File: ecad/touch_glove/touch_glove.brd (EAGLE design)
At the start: 78.3 x 40.6 mm, 177 parts, among them Q1 MCH3474 4A/30V, Q2 MCH3474 4A/30V, Q3 MCH3474 4A/30V, Q4 MCH3474 4A/30V, Q5 MCH3474 4A/30V, Q6 MCH3474 4A/30V, SW1 4A/28V

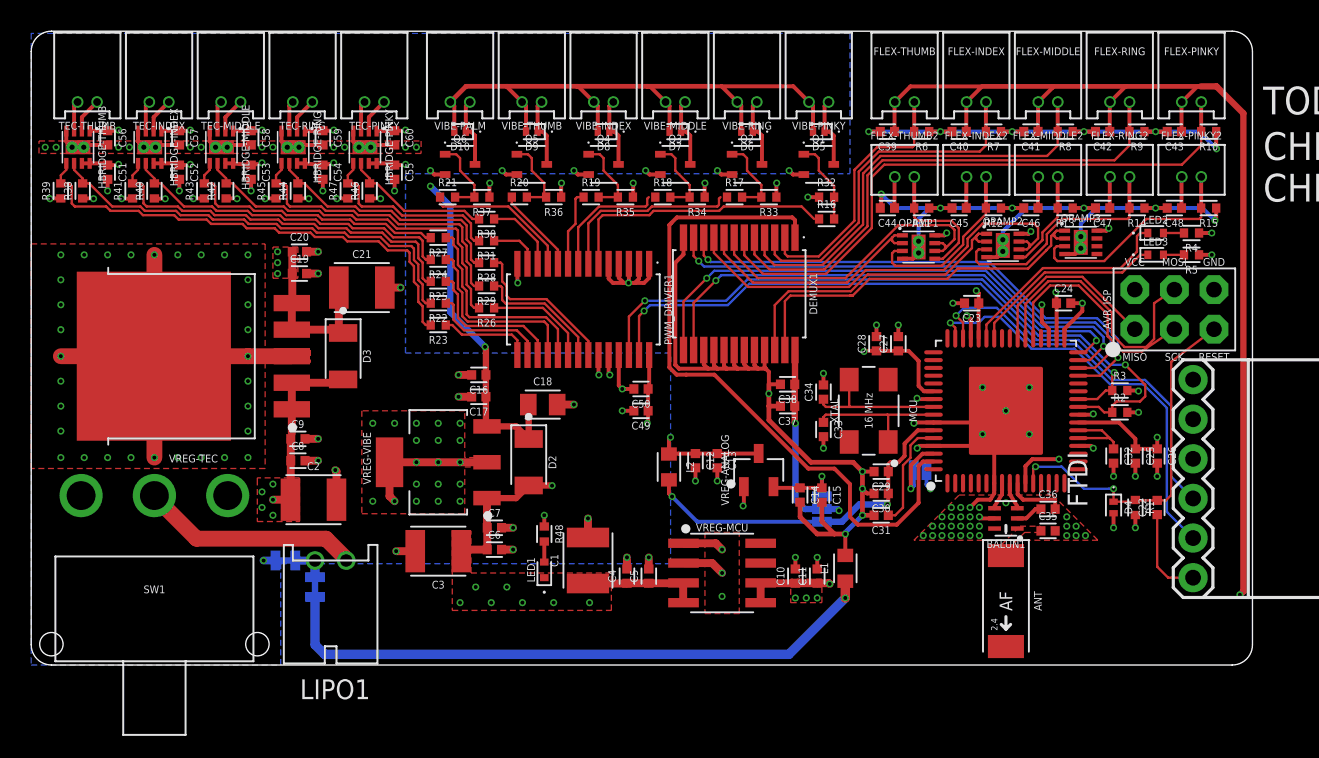
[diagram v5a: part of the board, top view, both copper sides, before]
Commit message: Update all components to new libraries.
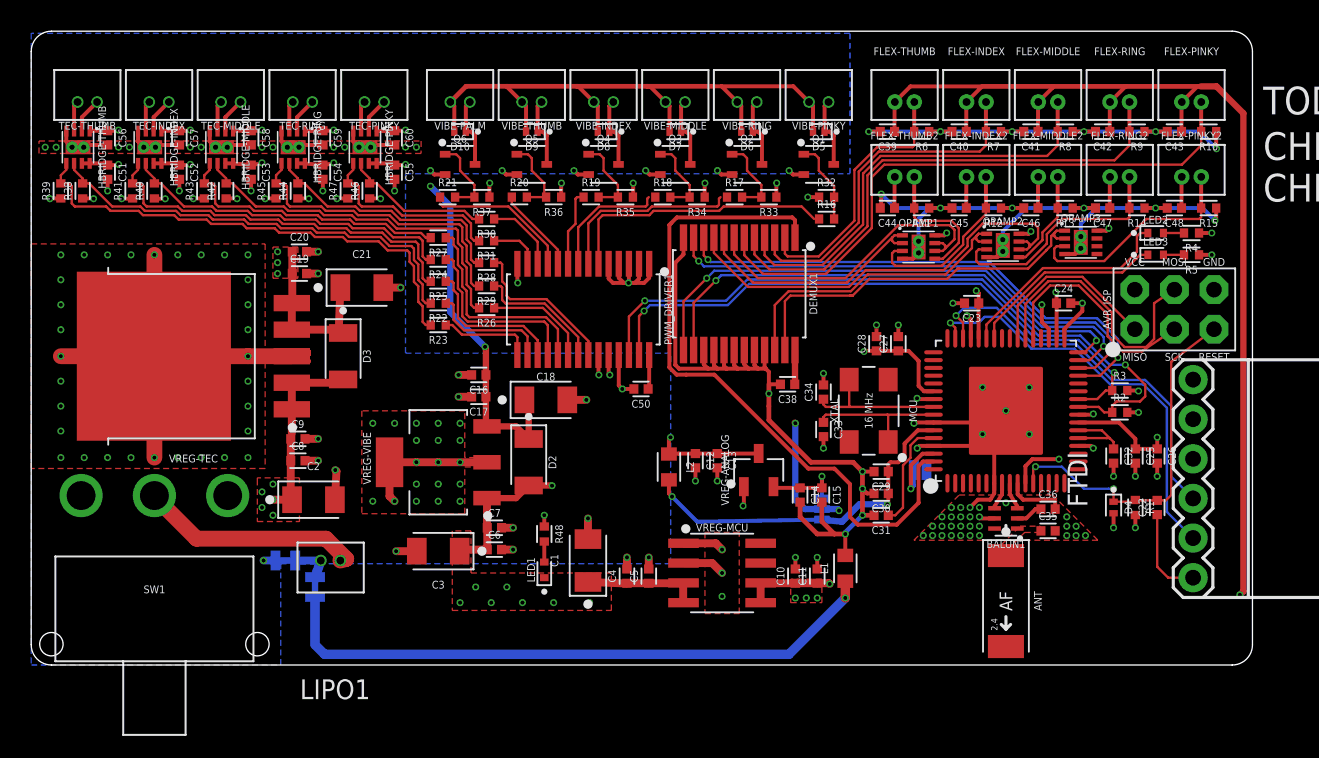
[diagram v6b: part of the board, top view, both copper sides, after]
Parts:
- removed C37, C49: 10uF/6.3V, PiB_capacitors:CAPC1005X55_SMD-0402
- ANT: device PiB_radio_frequency:ANTC6522X100 -> _radio_frequency:ANTC6522X100
- AVR_ISP: device PiB_connectors:HDRV6W64P254_2X3_762X483X838B_AVR-ISP -> _connectors:HDRV6W64P254_2X3_762X483X838B_AVR-ISP
- BALUN1: device PiB_radio_frequency:RESCAXE65P200X125X95-6 -> _radio_frequency:RESCAXE65P200X125X95-6
- BR_ANALOG, BR_NOISE: value 2PT_GND_TIE -> NET_BRIDGE; device PiB_power_symbols:2PT_GND_TIE -> _power_symbols:NET_BRIDGE
- C1, C2, C21, C3: device PiB_capacitors:CAPC3225X270_SMD-1210 -> _capacitors:CAPCP3216X160
- C10, C11, C12, C13, C14, C15, C16, C17, C19, C20, C22, C23, C24, C25, C26, C27, C28, C29, C30, C31, C32, C33, C34, C35, C36, C38, C39, C4, C40, C41, C42, C43, C44, C45, C46, C47, C48, C5, C50, C51, C52, C53, C54, C55, C56, C57, C58, C59, C6, C60, C7, C8, C9: device PiB_capacitors:CAPC1005X55_SMD-0402 -> _capacitors:CAPC1005X55_SMD-0402
- C18: value 47uF/6.3V -> 100uF/10V; device PiB_capacitors:CAPC2012X95_SMD-0805 -> _capacitors:CAPCP3216X160
- D10, D4, D5, D6, D7, D8, D9: device PiB_discrete_semiconductors:DFN100X60X55-2 -> _discrete_semiconductors:DFN100X60X55-2
- D2, D3: device PiB_discrete_semiconductors:SODFL3516X170 -> _discrete_semiconductors:SODFL3516X170
- DEMUX1: device PiB:SOP65P780X200-24 -> _special:SOP65P780X200-24
- FLEX-INDEX, FLEX-MIDDLE, FLEX-PINKY, FLEX-RING, FLEX-THUMB: device PiB_sensors:_MOLEX-0530480210_RA_PITCH-1.25MM -> _sensors:_MOLEX-0530470210_VERT_PITCH-1.25MM
- FLEX-INDEX2, FLEX-MIDDLE2, FLEX-PINKY2, FLEX-RING2, FLEX-THUMB2: device PiB_sensors:_MOLEX-0530470210_VERT_PITCH-1.25MM -> _sensors:_MOLEX-0530470210_VERT_PITCH-1.25MM
- FTDI: device PiB_connectors:FTDI_BASIC-6PIN-MALE-RA -> _connectors:FTDI_BASIC-6PIN-MALE-RA
- HBRIDGE-INDEX, HBRIDGE-MIDDLE, HBRIDGE-PINKY, HBRIDGE-RING, HBRIDGE-THUMB: device PiB:WSON-8-PPAD -> _special:WSON-8-PPAD
- JP1: value JUMPER_SMD_3-PAD_NO_NO-SILK -> JUMPER_SMD_3-PAD_NO_SILK; device PiB_connectors:SMT-JUMPER_3_NO_NO-SILK -> _connectors:SMT-JUMPER_3_NO_SILK
- JP2: device PiB_connectors:SMT-JUMPER_2_NO_SILK -> _connectors:SMT-JUMPER_2_NO_SILK
- L1, L2: device PiB_inductors:INDC1608X60-0603 -> _inductors:INDC1608X60-0603
- LED1, LED2, LED3: device PiB_leds:LEDC1005X40_LED-0402 -> _leds:LEDC1005X40_LED-0402
- LIPO1: device PiB_batteries:BATTERY_MOLEX-89401_RA_PITCH-2MM -> _batteries:BATTERY_MOLEX-0530470210_VERT_PITCH-1.25MM
- MCU: device PiB_ic_microcontrollers:QFN50P900X900X90-64 -> _ic_microcontrollers:QFN50P900X900X90-64
- OPAMP1, OPAMP2, OPAMP3: device PiB_op_amps:WSON-8-PPAD -> _op_amps:WSON-8-PPAD
- PWM_DRIVER1: device PiB:SOP65P650X110-28 -> _special:SOP65P650X110-28
- Q1, Q2, Q3, Q4, Q5, Q6: device PiB_discrete_semiconductors:SOTFL65P209X90-3 -> _transistors:SOTFL65P209X90-3
- R1, R10, R11, R12, R13, R14, R15, R16, R17, R18, R19, R2, R20, R21, R22, R23, R24, R25, R26, R27, R28, R29, R3, R30, R31, R32, R33, R34, R35, R36, R37, R38, R39, R4, R40, R41, R42, R43, R44, R45, R46, R47, R48, R5, R6, R7, R8, R9: device PiB_resistors:RESC1005X35_SMD-0402 -> _resistors:RESC1005X35_SMD-0402
- SW1: device PiB_switches:SW_SLIDE_SPDT_RA_PTH_12.7L-9.5W -> _switches:SW_SLIDE_SPDT_RA_PTH_12.7L-9.5W
- TEC-INDEX, TEC-MIDDLE, TEC-PINKY, TEC-RING, TEC-THUMB: value Molex RA 1.25mm pitch -> PELTIER; device PiB_actuators:_MOLEX-0530480210_RA_PITCH-1.25MM -> _actuators:_MOLEX-0530470210_VERT_PITCH-1.25MM
- VIBE-INDEX, VIBE-MIDDLE, VIBE-PALM, VIBE-PINKY, VIBE-RING, VIBE-THUMB: value Molex RA 1.25mm pitch -> Molex VERT 1.25mm pitch; device PiB_actuators:_MOLEX-0530480210_RA_PITCH-1.25MM -> _actuators:_MOLEX-0530470210_VERT_PITCH-1.25MM
- VREG-ANALOG: device PiB_ic_power:SOT95P237X112-3_SOT-23-3 -> _ic_power:SOT95P237X112-3_SOT-23-3
- VREG-MCU: value 1A/3.3V -> TPS76833QDR 1A/3.3V; device PiB_ic_power:SOIC127P600X265-8 -> _ic_power:SOIC127P600X265-8
- VREG-TEC: device PiB_ic_power:TO170P1363X457-6 -> _ic_power:TO170P1363X457-6
- VREG-VIBE: device PiB_ic_power:SOT229P700X180-4 -> _ic_power:SOT229P700X180-4
- XTAL: device PiB:OSCCC500X320X110 -> _crystals_oscillators_resonators:OSCCC500X320X110_CRYSTAL
- moved C18 0.36 mm to (33.0, 17.0)
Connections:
- net 1.8V: now also C21.A; no longer C21.1
- net 3.3V: now also C18.A; no longer C18.1
- net AGND: no longer C37.2
- net GND: no longer C49.2
- net NGND: now also C1.K, C18.K, C2.K, C21.K, C3.K; no longer C1.2, C18.2, C2.2, C21.2, C3.2
- net VBAT: now also C1.A, C2.A, C3.A; no longer C1.1, C2.1, C3.1
- net VCC: no longer C49.1
- net VSENSOR: no longer C37.1
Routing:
- net VSENSOR: track 178.9 -> 176.5 mm
- net VCC: track 51.7 -> 49.4 mm, vias 19 -> 18
- net AGND: track 227.7 -> 227.0 mm
- net 3.3V: track 70.0 -> 70.5 mm
- net GND: track 66.1 -> 65.8 mm, vias 52 -> 51

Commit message: Fix all errors on board.
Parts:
- moved AVR_ISP 0.10 mm to (70.8, 21.4)
- moved C17 0.10 mm to (28.7, 17.3)
- moved FLEX-INDEX 0.10 mm to (60.6, 36.2)
- moved FLEX-MIDDLE 0.10 mm to (65.2, 36.2)
- moved FLEX-PINKY 0.10 mm to (74.4, 36.2)
- moved FLEX-RING 0.10 mm to (69.8, 36.2)
- moved FLEX-THUMB 0.10 mm to (56.0, 36.2)
- moved TEC-INDEX 0.10 mm to (8.20, 36.2)
- moved TEC-MIDDLE 0.10 mm to (12.8, 36.2)
- moved TEC-PINKY 0.10 mm to (22.0, 36.2)
- moved TEC-RING 0.10 mm to (17.4, 36.2)
- moved TEC-THUMB 0.10 mm to (3.60, 36.2)
- moved VIBE-INDEX 0.10 mm to (36.7, 36.2)
- moved VIBE-MIDDLE 0.10 mm to (41.3, 36.2)
- moved VIBE-PALM 0.10 mm to (27.5, 36.2)
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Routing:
- net VSENSOR: track 176.5 -> 180.0 mm
- net VCC: track 49.4 -> 50.3 mm, vias 18 -> 19
- net 3.3V: track 70.5 -> 71.2 mm

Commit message: Completed most of the circuitry for the ET schematic.
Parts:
- added C37, C49, C63, C64, C66, C67, C68, C69, C70, C76, C78, C80: 0.1uF/50V, _capacitors:CAPC1005X55_SMD-0402
- added C61: 0.1uF/25V, _capacitors:CAPC1608X95
- added C62: 0.1uF/250V, _capacitors:CAPC2012X95_SMD-0805
- added C65: 100uF/10V, _capacitors:CAPCP3216X160
- added C71, C72, C73, C75, C77, C79: 10uF/6.3V, _capacitors:CAPC1005X55_SMD-0402
- added C74: 4.7uF/10V/0402, _capacitors:CAPC1005X55_SMD-0402
- added ET_INDEX_PIXEL1-1, ET_INDEX_PIXEL1-10, ET_INDEX_PIXEL1-11, ET_INDEX_PIXEL1-12, ET_INDEX_PIXEL1-13, ET_INDEX_PIXEL1-14, ET_INDEX_PIXEL1-15, ET_INDEX_PIXEL1-16, ET_INDEX_PIXEL1-17, ET_INDEX_PIXEL1-18, ET_INDEX_PIXEL1-19, ET_INDEX_PIXEL1-2, ET_INDEX_PIXEL1-20, ET_INDEX_PIXEL1-3, ET_INDEX_PIXEL1-4, ET_INDEX_PIXEL1-5, ET_INDEX_PIXEL1-6, ET_INDEX_PIXEL1-7, ET_INDEX_PIXEL1-8, ET_INDEX_PIXEL1-9, ET_INDEX_PIXEL2-1, ET_INDEX_PIXEL2-10, ET_INDEX_PIXEL2-11, ET_INDEX_PIXEL2-12, ET_INDEX_PIXEL2-13, ET_INDEX_PIXEL2-14, ET_INDEX_PIXEL2-15, ET_INDEX_PIXEL2-16, ET_INDEX_PIXEL2-17, ET_INDEX_PIXEL2-18, ET_INDEX_PIXEL2-19, ET_INDEX_PIXEL2-2, ET_INDEX_PIXEL2-20, ET_INDEX_PIXEL2-3, ET_INDEX_PIXEL2-4, ET_INDEX_PIXEL2-5, ET_INDEX_PIXEL2-6, ET_INDEX_PIXEL2-7, ET_INDEX_PIXEL2-8, ET_INDEX_PIXEL2-9, ET_INDEX_PIXEL3-1, ET_INDEX_PIXEL3-10, ET_INDEX_PIXEL3-11, ET_INDEX_PIXEL3-12, ET_INDEX_PIXEL3-13, ET_INDEX_PIXEL3-14, ET_INDEX_PIXEL3-15, ET_INDEX_PIXEL3-16, ET_INDEX_PIXEL3-17, ET_INDEX_PIXEL3-18, ET_INDEX_PIXEL3-19, ET_INDEX_PIXEL3-2, ET_INDEX_PIXEL3-20, ET_INDEX_PIXEL3-3, ET_INDEX_PIXEL3-4, ET_INDEX_PIXEL3-5, ET_INDEX_PIXEL3-6, ET_INDEX_PIXEL3-7, ET_INDEX_PIXEL3-8, ET_INDEX_PIXEL3-9, ET_INDEX_PIXEL4-1, ET_INDEX_PIXEL4-10, ET_INDEX_PIXEL4-11, ET_INDEX_PIXEL4-12, ET_INDEX_PIXEL4-13, ET_INDEX_PIXEL4-14, ET_INDEX_PIXEL4-15, ET_INDEX_PIXEL4-16, ET_INDEX_PIXEL4-17, ET_INDEX_PIXEL4-18, ET_INDEX_PIXEL4-19, ET_INDEX_PIXEL4-2, ET_INDEX_PIXEL4-20, ET_INDEX_PIXEL4-3, ET_INDEX_PIXEL4-4, ET_INDEX_PIXEL4-5, ET_INDEX_PIXEL4-6, ET_INDEX_PIXEL4-7, ET_INDEX_PIXEL4-8, ET_INDEX_PIXEL4-9: SPST-NO 170mA 250V, _relay:SOP254P609X203-4
- added IC1: DRV8662, _special:QFN50P400X400X100-21T270
- added J1, J2, J3, J4, J5: VERT MALE 2.54MM, _connectors:HDRV16W64P254_1X16_4064X254X838B
- added J6, J7, J8, J9: PTH VERT MALE, _connectors:HDRV2W64P254_1X2_508X254X838B
- added L3: 4.7uH/1.4A, _inductors:INDC2520X100
- added L4: 10uH/380mA, _inductors:INDC1608X60-0603
- added NFET1: 2N7002DW, _transistors:SOT65P230X110-6
- added OPAMP4: TLV2361_GP_20MA_7MHZ, _op_amps:SOT95P280X145-5
- added POT1: 100K, _resistors:POTENTIOMETER_SQ-L5-W4.5-H2.3
- added PWM_DRIVER2, PWM_DRIVER3, PWM_DRIVER4, PWM_DRIVER5, PWM_DRIVER6: PCA9685, _special:SOP65P650X110-28
- added R100, R101, R102, R103, R104, R105, R106, R107, R108, R109, R110, R111, R112, R113, R114, R115, R116, R117, R118, R119, R120, R121, R122, R123, R124, R125, R126, R127, R128, R129, R130, R131, R132, R133, R134, R135, R49, R57, R58, R59, R60, R61, R62, R63, R64, R65, R66, R67, R68, R69, R70, R71, R72, R73, R74, R75, R76, R77, R78, R79, R80, R81, R82, R83, R84, R85, R86, R87, R88, R89, R90, R91, R92, R93, R94, R95, R96, R97, R98, R99: 1K, _resistors:RESC1005X35_SMD-0402
- added R136, R137, R54, R55, R56: 10K, _resistors:RESC1005X35_SMD-0402
- added R50: 768K, _resistors:RESC1005X35_SMD-0402
- added R51: 35.7K, _resistors:RESC1005X35_SMD-0402
- added R52: 20K, _resistors:RESC1005X35_SMD-0402
- added R53: 41.2K, _resistors:RESC1005X35_SMD-0402
- added REXT: 7.5K, _resistors:RESC1005X35_SMD-0402
- added SW2: 25mA/24V, _switches:SW_SLIDE_ARRAY-3_L9.6-W7.5-H4.5
- added VREG-MCU1: TPS76833QDR 1A/3.3V, _ic_power:SOIC127P600X265-8
- added VREG2: NCP1729 50mA, _ic_power:SOT95P275X100-6
- added VREG3: TPS62202 300mA 1.8V, _ic_power:SOT95P280X145-5
- moved C21 0.57 mm to (20.8, 23.8)
- moved D3 0.40 mm to (19.6, 19.8)
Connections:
- new net -1.8V: C72.1, OPAMP4.2, VREG2.1
- new net C+: C71.1, VREG2.6
- new net C-: C71.2, VREG2.3
- new net EN: IC1.20, R54.2, SW2.S3
- new net FB: IC1.3, R50.1, R51.2, R52.2, R53.2
- new net GAIN0: IC1.18, NFET1.5, R55.2, SW2.S2
- new net GAIN1: IC1.19, NFET1.2, R56.2, SW2.S1
- new net IN+: C64.1, OPAMP4.4, POT1.1, POT1.2, R136.2
- new net INDEX_IN1-1: ET_INDEX_PIXEL1-1.1, ET_INDEX_PIXEL1-13.1, ET_INDEX_PIXEL1-17.1, ET_INDEX_PIXEL1-5.1, ET_INDEX_PIXEL1-9.1, PWM_DRIVER2.6, PWM_DRIVER3.6, PWM_DRIVER4.6, PWM_DRIVER5.6, PWM_DRIVER6.6
- new net INDEX_IN1-2: ET_INDEX_PIXEL1-10.1, ET_INDEX_PIXEL1-14.1, ET_INDEX_PIXEL1-18.1, ET_INDEX_PIXEL1-2.1, ET_INDEX_PIXEL1-6.1, PWM_DRIVER2.7, PWM_DRIVER3.7, PWM_DRIVER4.7, PWM_DRIVER5.7, PWM_DRIVER6.7
- new net INDEX_IN1-3: ET_INDEX_PIXEL1-11.1, ET_INDEX_PIXEL1-15.1, ET_INDEX_PIXEL1-19.1, ET_INDEX_PIXEL1-3.1, ET_INDEX_PIXEL1-7.1, PWM_DRIVER2.8, PWM_DRIVER3.8, PWM_DRIVER4.8, PWM_DRIVER5.8, PWM_DRIVER6.8
- new net INDEX_IN1-4: ET_INDEX_PIXEL1-12.1, ET_INDEX_PIXEL1-16.1, ET_INDEX_PIXEL1-20.1, ET_INDEX_PIXEL1-4.1, ET_INDEX_PIXEL1-8.1, PWM_DRIVER2.9, PWM_DRIVER3.9, PWM_DRIVER4.9, PWM_DRIVER5.9, PWM_DRIVER6.9
- new net INDEX_IN2-1: ET_INDEX_PIXEL2-1.1, ET_INDEX_PIXEL2-11.1, ET_INDEX_PIXEL2-15.1, ET_INDEX_PIXEL2-19.1, ET_INDEX_PIXEL2-7.1, PWM_DRIVER2.10, PWM_DRIVER3.10, PWM_DRIVER4.10, PWM_DRIVER5.10, PWM_DRIVER6.10
- new net INDEX_IN2-2: ET_INDEX_PIXEL2-10.1, ET_INDEX_PIXEL2-14.1, ET_INDEX_PIXEL2-18.1, ET_INDEX_PIXEL2-2.1, ET_INDEX_PIXEL2-6.1, PWM_DRIVER2.11, PWM_DRIVER3.11, PWM_DRIVER4.11, PWM_DRIVER5.11, PWM_DRIVER6.11
- new net INDEX_IN2-3: ET_INDEX_PIXEL2-13.1, ET_INDEX_PIXEL2-17.1, ET_INDEX_PIXEL2-3.1, ET_INDEX_PIXEL2-5.1, ET_INDEX_PIXEL2-9.1, PWM_DRIVER2.12, PWM_DRIVER3.12, PWM_DRIVER4.12, PWM_DRIVER5.12, PWM_DRIVER6.12
- new net INDEX_IN2-4: ET_INDEX_PIXEL2-12.1, ET_INDEX_PIXEL2-16.1, ET_INDEX_PIXEL2-20.1, ET_INDEX_PIXEL2-4.1, ET_INDEX_PIXEL2-8.1, PWM_DRIVER2.13, PWM_DRIVER3.13, PWM_DRIVER4.13, PWM_DRIVER5.13, PWM_DRIVER6.13
- new net INDEX_IN3-1: ET_INDEX_PIXEL3-1.1, ET_INDEX_PIXEL3-13.1, ET_INDEX_PIXEL3-17.1, ET_INDEX_PIXEL3-5.1, ET_INDEX_PIXEL3-9.1, PWM_DRIVER2.15, PWM_DRIVER3.15, PWM_DRIVER4.15, PWM_DRIVER5.15, PWM_DRIVER6.15
- new net INDEX_IN3-2: ET_INDEX_PIXEL3-10.1, ET_INDEX_PIXEL3-14.1, ET_INDEX_PIXEL3-18.1, ET_INDEX_PIXEL3-2.1, ET_INDEX_PIXEL3-6.1, PWM_DRIVER2.16, PWM_DRIVER3.16, PWM_DRIVER4.16, PWM_DRIVER5.16, PWM_DRIVER6.16
- new net INDEX_IN3-3: ET_INDEX_PIXEL3-11.1, ET_INDEX_PIXEL3-15.1, ET_INDEX_PIXEL3-19.1, ET_INDEX_PIXEL3-3.1, ET_INDEX_PIXEL3-7.1, PWM_DRIVER2.17, PWM_DRIVER3.17, PWM_DRIVER4.17, PWM_DRIVER5.17, PWM_DRIVER6.17
- new net INDEX_IN3-4: ET_INDEX_PIXEL3-12.1, ET_INDEX_PIXEL3-16.1, ET_INDEX_PIXEL3-20.1, ET_INDEX_PIXEL3-4.1, ET_INDEX_PIXEL3-8.1, PWM_DRIVER2.18, PWM_DRIVER3.18, PWM_DRIVER4.18, PWM_DRIVER5.18, PWM_DRIVER6.18
- new net INDEX_IN4-1: ET_INDEX_PIXEL4-1.1, ET_INDEX_PIXEL4-13.1, ET_INDEX_PIXEL4-17.1, ET_INDEX_PIXEL4-5.1, ET_INDEX_PIXEL4-9.1, PWM_DRIVER2.19, PWM_DRIVER3.19, PWM_DRIVER4.19, PWM_DRIVER5.19, PWM_DRIVER6.19
- new net INDEX_IN4-2: ET_INDEX_PIXEL4-10.1, ET_INDEX_PIXEL4-14.1, ET_INDEX_PIXEL4-18.1, ET_INDEX_PIXEL4-2.1, ET_INDEX_PIXEL4-6.1, PWM_DRIVER2.20, PWM_DRIVER3.20, PWM_DRIVER4.20, PWM_DRIVER5.20, PWM_DRIVER6.20
- new net INDEX_IN4-3: ET_INDEX_PIXEL4-11.1, ET_INDEX_PIXEL4-15.1, ET_INDEX_PIXEL4-19.1, ET_INDEX_PIXEL4-3.1, ET_INDEX_PIXEL4-7.1, PWM_DRIVER2.21, PWM_DRIVER3.21, PWM_DRIVER4.21, PWM_DRIVER5.21, PWM_DRIVER6.21
- new net INDEX_IN4-4: ET_INDEX_PIXEL4-12.1, ET_INDEX_PIXEL4-16.1, ET_INDEX_PIXEL4-20.1, ET_INDEX_PIXEL4-4.1, ET_INDEX_PIXEL4-8.1, PWM_DRIVER2.22, PWM_DRIVER3.22, PWM_DRIVER4.22, PWM_DRIVER5.22, PWM_DRIVER6.22
- new net INDEX_OUT1-1: ET_INDEX_PIXEL1-1.3, ET_INDEX_PIXEL1-13.3, ET_INDEX_PIXEL1-17.3, ET_INDEX_PIXEL1-5.3, ET_INDEX_PIXEL1-9.3, J1.1, J2.1, J3.1, J4.1, J5.1
- new net INDEX_OUT1-2: ET_INDEX_PIXEL1-10.3, ET_INDEX_PIXEL1-14.3, ET_INDEX_PIXEL1-18.3, ET_INDEX_PIXEL1-2.3, ET_INDEX_PIXEL1-6.3
- new net INDEX_OUT1-3: ET_INDEX_PIXEL1-11.3, ET_INDEX_PIXEL1-15.3, ET_INDEX_PIXEL1-19.3, ET_INDEX_PIXEL1-3.3, ET_INDEX_PIXEL1-7.3
- new net INDEX_OUT1-4: ET_INDEX_PIXEL1-12.3, ET_INDEX_PIXEL1-16.3, ET_INDEX_PIXEL1-20.3, ET_INDEX_PIXEL1-4.3, ET_INDEX_PIXEL1-8.3
- new net INDEX_OUT2-1: ET_INDEX_PIXEL2-1.3, ET_INDEX_PIXEL2-11.3, ET_INDEX_PIXEL2-15.3, ET_INDEX_PIXEL2-19.3, ET_INDEX_PIXEL2-7.3
- new net INDEX_OUT2-2: ET_INDEX_PIXEL2-10.3, ET_INDEX_PIXEL2-14.3, ET_INDEX_PIXEL2-18.3, ET_INDEX_PIXEL2-2.3, ET_INDEX_PIXEL2-6.3
- new net INDEX_OUT2-3: ET_INDEX_PIXEL2-13.3, ET_INDEX_PIXEL2-17.3, ET_INDEX_PIXEL2-3.3, ET_INDEX_PIXEL2-5.3, ET_INDEX_PIXEL2-9.3
- new net INDEX_OUT2-4: ET_INDEX_PIXEL2-12.3, ET_INDEX_PIXEL2-16.3, ET_INDEX_PIXEL2-20.3, ET_INDEX_PIXEL2-4.3, ET_INDEX_PIXEL2-8.3
- new net INDEX_OUT3-1: ET_INDEX_PIXEL3-1.3, ET_INDEX_PIXEL3-13.3, ET_INDEX_PIXEL3-17.3, ET_INDEX_PIXEL3-5.3, ET_INDEX_PIXEL3-9.3
- new net INDEX_OUT3-2: ET_INDEX_PIXEL3-10.3, ET_INDEX_PIXEL3-14.3, ET_INDEX_PIXEL3-18.3, ET_INDEX_PIXEL3-2.3, ET_INDEX_PIXEL3-6.3
- new net INDEX_OUT3-3: ET_INDEX_PIXEL3-11.3, ET_INDEX_PIXEL3-15.3, ET_INDEX_PIXEL3-19.3, ET_INDEX_PIXEL3-3.3, ET_INDEX_PIXEL3-7.3
- new net INDEX_OUT3-4: ET_INDEX_PIXEL3-12.3, ET_INDEX_PIXEL3-16.3, ET_INDEX_PIXEL3-20.3, ET_INDEX_PIXEL3-4.3, ET_INDEX_PIXEL3-8.3
- new net INDEX_OUT4-1: ET_INDEX_PIXEL4-1.3, ET_INDEX_PIXEL4-13.3, ET_INDEX_PIXEL4-17.3, ET_INDEX_PIXEL4-5.3, ET_INDEX_PIXEL4-9.3
- new net INDEX_OUT4-2: ET_INDEX_PIXEL4-10.3, ET_INDEX_PIXEL4-14.3, ET_INDEX_PIXEL4-18.3, ET_INDEX_PIXEL4-2.3, ET_INDEX_PIXEL4-6.3
- new net INDEX_OUT4-3: ET_INDEX_PIXEL4-11.3, ET_INDEX_PIXEL4-15.3, ET_INDEX_PIXEL4-19.3, ET_INDEX_PIXEL4-3.3, ET_INDEX_PIXEL4-7.3
- new net INDEX_OUT4-4: ET_INDEX_PIXEL4-12.3, ET_INDEX_PIXEL4-16.3, ET_INDEX_PIXEL4-20.3, ET_INDEX_PIXEL4-4.3, ET_INDEX_PIXEL4-8.3
- new net N$100: ET_INDEX_PIXEL3-12.2, R99.2
- new net N$101: ET_INDEX_PIXEL4-9.2, R100.2
- new net N$102: ET_INDEX_PIXEL4-10.2, R101.2
- new net N$103: ET_INDEX_PIXEL4-11.2, R102.2
- new net N$104: ET_INDEX_PIXEL4-12.2, R103.2
- new net N$105: ET_INDEX_PIXEL1-13.2, R104.2
- new net N$106: ET_INDEX_PIXEL1-14.2, R105.2
- new net N$107: ET_INDEX_PIXEL1-15.2, R106.2
- new net N$108: ET_INDEX_PIXEL1-16.2, R107.2
- new net N$109: ET_INDEX_PIXEL2-15.2, R108.2
- new net N$110: ET_INDEX_PIXEL2-14.2, R109.2
- new net N$111: ET_INDEX_PIXEL2-13.2, R110.2
- new net N$112: ET_INDEX_PIXEL2-16.2, R111.2
- new net N$113: ET_INDEX_PIXEL3-13.2, R112.2
- new net N$114: ET_INDEX_PIXEL3-14.2, R113.2
- new net N$115: ET_INDEX_PIXEL3-15.2, R114.2
- new net N$116: ET_INDEX_PIXEL3-16.2, R115.2
- new net N$117: ET_INDEX_PIXEL4-13.2, R116.2
- new net N$118: ET_INDEX_PIXEL4-14.2, R117.2
- new net N$119: ET_INDEX_PIXEL4-15.2, R118.2
- new net N$120: ET_INDEX_PIXEL4-16.2, R119.2
- new net N$121: ET_INDEX_PIXEL1-17.2, R120.2
- new net N$122: ET_INDEX_PIXEL1-18.2, R121.2
- new net N$123: ET_INDEX_PIXEL1-19.2, R122.2
- new net N$124: ET_INDEX_PIXEL1-20.2, R123.2
- new net N$125: ET_INDEX_PIXEL2-19.2, R124.2
- new net N$126: ET_INDEX_PIXEL2-18.2, R125.2
- new net N$127: ET_INDEX_PIXEL2-17.2, R126.2
- new net N$128: ET_INDEX_PIXEL2-20.2, R127.2
- new net N$129: ET_INDEX_PIXEL3-17.2, R128.2
- new net N$130: ET_INDEX_PIXEL3-18.2, R129.2
- new net N$131: ET_INDEX_PIXEL3-19.2, R130.2
- new net N$132: ET_INDEX_PIXEL3-20.2, R131.2
- new net N$133: ET_INDEX_PIXEL4-17.2, R132.2
- new net N$134: ET_INDEX_PIXEL4-18.2, R133.2
- new net N$135: ET_INDEX_PIXEL4-19.2, R134.2
- new net N$136: ET_INDEX_PIXEL4-20.2, R135.2
- new net N$137: L4.1, VREG3.5
- new net N$138: OPAMP4.1, R136.1, R137.2
- new net N$139: C76.1, OPAMP4.3, POT1.3
- new net N$33: ET_INDEX_PIXEL1-3.2, R58.2
- new net N$39: ET_INDEX_PIXEL1-1.2, R49.2
- new net N$42: IC1.7, IC1.8, L3.1
- new net N$43: C49.1, IC1.1
- new net N$44: C62.1, IC1.10, IC1.11, IC1.12, R50.2
- new net N$48: IC1.15, REXT.2
- new net N$49: NFET1.6, R52.1
- new net N$51: NFET1.3, R53.1
- new net N$52: C64.2, IC1.17
- new net N$56: C63.2, IC1.16
- new net N$57: ET_INDEX_PIXEL1-2.2, R57.2
- new net N$58: ET_INDEX_PIXEL1-5.2, R72.2
- new net N$59: ET_INDEX_PIXEL1-4.2, R59.2
- new net N$60: ET_INDEX_PIXEL2-1.2, R60.2
- new net N$61: ET_INDEX_PIXEL2-2.2, R61.2
- new net N$64: ET_INDEX_PIXEL2-3.2, R62.2
- new net N$65: ET_INDEX_PIXEL2-4.2, R63.2
- new net N$66: ET_INDEX_PIXEL3-1.2, R64.2
- new net N$67: ET_INDEX_PIXEL3-2.2, R65.2
- new net N$68: ET_INDEX_PIXEL3-3.2, R66.2
- new net N$69: ET_INDEX_PIXEL3-4.2, R67.2
- new net N$70: ET_INDEX_PIXEL4-1.2, R68.2
- new net N$71: ET_INDEX_PIXEL4-2.2, R69.2
- new net N$72: ET_INDEX_PIXEL4-3.2, R70.2
- new net N$73: ET_INDEX_PIXEL4-4.2, R71.2
- new net N$74: ET_INDEX_PIXEL1-6.2, R73.2
- new net N$75: ET_INDEX_PIXEL1-7.2, R74.2
- new net N$76: ET_INDEX_PIXEL1-8.2, R75.2
- new net N$77: ET_INDEX_PIXEL2-7.2, R76.2
- new net N$78: ET_INDEX_PIXEL2-6.2, R77.2
- new net N$79: ET_INDEX_PIXEL2-5.2, R78.2
- new net N$80: ET_INDEX_PIXEL2-8.2, R79.2
- new net N$81: ET_INDEX_PIXEL3-5.2, R80.2
- new net N$82: ET_INDEX_PIXEL3-6.2, R81.2
- new net N$83: ET_INDEX_PIXEL3-7.2, R82.2
- new net N$84: ET_INDEX_PIXEL3-8.2, R83.2
- new net N$85: ET_INDEX_PIXEL4-5.2, R84.2
- new net N$86: ET_INDEX_PIXEL4-6.2, R85.2
- new net N$87: ET_INDEX_PIXEL4-7.2, R86.2
- new net N$88: ET_INDEX_PIXEL4-8.2, R87.2
- new net N$89: ET_INDEX_PIXEL1-9.2, R88.2
- new net N$90: ET_INDEX_PIXEL1-10.2, R89.2
- new net N$91: ET_INDEX_PIXEL1-11.2, R90.2
- new net N$92: ET_INDEX_PIXEL1-12.2, R91.2
- new net N$93: ET_INDEX_PIXEL2-11.2, R92.2
- new net N$94: ET_INDEX_PIXEL2-10.2, R93.2
- new net N$95: ET_INDEX_PIXEL2-9.2, R94.2
- new net N$96: ET_INDEX_PIXEL2-12.2, R95.2
- new net N$97: ET_INDEX_PIXEL3-9.2, R96.2
- new net N$98: ET_INDEX_PIXEL3-10.2, R97.2
- new net N$99: ET_INDEX_PIXEL3-11.2, R98.2
- new net V+: ET_INDEX_PIXEL1-1.4, ET_INDEX_PIXEL1-10.4, ET_INDEX_PIXEL1-11.4, ET_INDEX_PIXEL1-12.4, ET_INDEX_PIXEL1-13.4, ET_INDEX_PIXEL1-14.4, ET_INDEX_PIXEL1-15.4, ET_INDEX_PIXEL1-16.4, ET_INDEX_PIXEL1-17.4, ET_INDEX_PIXEL1-18.4, ET_INDEX_PIXEL1-19.4, ET_INDEX_PIXEL1-2.4, ET_INDEX_PIXEL1-20.4, ET_INDEX_PIXEL1-3.4, ET_INDEX_PIXEL1-4.4, ET_INDEX_PIXEL1-5.4, ET_INDEX_PIXEL1-6.4, ET_INDEX_PIXEL1-7.4, ET_INDEX_PIXEL1-8.4, ET_INDEX_PIXEL1-9.4, ET_INDEX_PIXEL2-1.4, ET_INDEX_PIXEL2-10.4, ET_INDEX_PIXEL2-11.4, ET_INDEX_PIXEL2-12.4, ET_INDEX_PIXEL2-13.4, ET_INDEX_PIXEL2-14.4, ET_INDEX_PIXEL2-15.4, ET_INDEX_PIXEL2-16.4, ET_INDEX_PIXEL2-17.4, ET_INDEX_PIXEL2-18.4, ET_INDEX_PIXEL2-19.4, ET_INDEX_PIXEL2-2.4, ET_INDEX_PIXEL2-20.4, ET_INDEX_PIXEL2-3.4, ET_INDEX_PIXEL2-4.4, ET_INDEX_PIXEL2-5.4, ET_INDEX_PIXEL2-6.4, ET_INDEX_PIXEL2-7.4, ET_INDEX_PIXEL2-8.4, ET_INDEX_PIXEL2-9.4, ET_INDEX_PIXEL3-1.4, ET_INDEX_PIXEL3-10.4, ET_INDEX_PIXEL3-11.4, ET_INDEX_PIXEL3-12.4, ET_INDEX_PIXEL3-13.4, ET_INDEX_PIXEL3-14.4, ET_INDEX_PIXEL3-15.4, ET_INDEX_PIXEL3-16.4, ET_INDEX_PIXEL3-17.4, ET_INDEX_PIXEL3-18.4, ET_INDEX_PIXEL3-19.4, ET_INDEX_PIXEL3-2.4, ET_INDEX_PIXEL3-20.4, ET_INDEX_PIXEL3-3.4, ET_INDEX_PIXEL3-4.4, ET_INDEX_PIXEL3-5.4, ET_INDEX_PIXEL3-6.4, ET_INDEX_PIXEL3-7.4, ET_INDEX_PIXEL3-8.4, ET_INDEX_PIXEL3-9.4, ET_INDEX_PIXEL4-1.4, ET_INDEX_PIXEL4-10.4, ET_INDEX_PIXEL4-11.4, ET_INDEX_PIXEL4-12.4, ET_INDEX_PIXEL4-13.4, ET_INDEX_PIXEL4-14.4, ET_INDEX_PIXEL4-15.4, ET_INDEX_PIXEL4-16.4, ET_INDEX_PIXEL4-17.4, ET_INDEX_PIXEL4-18.4, ET_INDEX_PIXEL4-19.4, ET_INDEX_PIXEL4-2.4, ET_INDEX_PIXEL4-20.4, ET_INDEX_PIXEL4-3.4, ET_INDEX_PIXEL4-4.4, ET_INDEX_PIXEL4-5.4, ET_INDEX_PIXEL4-6.4, ET_INDEX_PIXEL4-7.4, ET_INDEX_PIXEL4-8.4, ET_INDEX_PIXEL4-9.4, IC1.13
- new net V-: IC1.14, J1.16, J2.16, J3.16, J4.16, J5.16
- net 1.8V: now also C73.1, C75.1, L4.2, OPAMP4.5, VREG2.2, VREG2.5, VREG3.4
- net 3.3V: now also C37.1, C61.1, C65.A, C74.1, C77.1, C78.1, IC1.2, L3.2, SW2.P1, SW2.P2, SW2.P3, VREG-MCU1.5, VREG-MCU1.6, VREG3.1
- net GND: now also C37.2, C49.2, C61.2, C62.2, C63.1, C65.K, C66.2, C67.2, C68.2, C69.2, C70.2, C72.2, C73.2, C74.2, C75.2, C76.2, C77.2, C78.2, C79.2, C80.2, IC1.4, IC1.5, IC1.6, IC1.9, IC1.EP, IC1.P$1, IC1.P$2, IC1.P$3, IC1.P$4, NFET1.1, NFET1.4, PWM_DRIVER2.1, PWM_DRIVER2.14, PWM_DRIVER2.2, PWM_DRIVER2.23, PWM_DRIVER2.24, PWM_DRIVER2.25, PWM_DRIVER2.3, PWM_DRIVER2.4, PWM_DRIVER2.5, PWM_DRIVER3.1, PWM_DRIVER3.14, PWM_DRIVER3.2, PWM_DRIVER3.23, PWM_DRIVER3.24, PWM_DRIVER3.25, PWM_DRIVER3.3, PWM_DRIVER3.4, PWM_DRIVER3.5, PWM_DRIVER4.1, PWM_DRIVER4.14, PWM_DRIVER4.2, PWM_DRIVER4.23, PWM_DRIVER4.24, PWM_DRIVER4.25, PWM_DRIVER4.3, PWM_DRIVER4.4, PWM_DRIVER4.5, PWM_DRIVER5.1, PWM_DRIVER5.14, PWM_DRIVER5.2, PWM_DRIVER5.23, PWM_DRIVER5.24, PWM_DRIVER5.25, PWM_DRIVER5.3, PWM_DRIVER5.4, PWM_DRIVER5.5, PWM_DRIVER6.1, PWM_DRIVER6.14, PWM_DRIVER6.2, PWM_DRIVER6.23, PWM_DRIVER6.24, PWM_DRIVER6.25, PWM_DRIVER6.3, PWM_DRIVER6.4, PWM_DRIVER6.5, R100.1, R101.1, R102.1, R103.1, R104.1, R105.1, R106.1, R107.1, R108.1, R109.1, R110.1, R111.1, R112.1, R113.1, R114.1, R115.1, R116.1, R117.1, R118.1, R119.1, R120.1, R121.1, R122.1, R123.1, R124.1, R125.1, R126.1, R127.1, R128.1, R129.1, R130.1, R131.1, R132.1, R133.1, R134.1, R135.1, R137.1, R49.1, R51.1, R54.1, R55.1, R56.1, R57.1, R58.1, R59.1, R60.1, R61.1, R62.1, R63.1, R64.1, R65.1, R66.1, R67.1, R68.1, R69.1, R70.1, R71.1, R72.1, R73.1, R74.1, R75.1, R76.1, R77.1, R78.1, R79.1, R80.1, R81.1, R82.1, R83.1, R84.1, R85.1, R86.1, R87.1, R88.1, R89.1, R90.1, R91.1, R92.1, R93.1, R94.1, R95.1, R96.1, R97.1, R98.1, R99.1, REXT.1, VREG-MCU1.1, VREG-MCU1.2, VREG2.4, VREG3.2
- net N$7: now also VREG3.3
- net SCL: now also PWM_DRIVER2.26, PWM_DRIVER3.26, PWM_DRIVER4.26, PWM_DRIVER5.26, PWM_DRIVER6.26
- net SDA: now also PWM_DRIVER2.27, PWM_DRIVER3.27, PWM_DRIVER4.27, PWM_DRIVER5.27, PWM_DRIVER6.27
- net VBAT: now also C79.1, C80.1, VREG-MCU1.3, VREG-MCU1.4
- net VCC: now also C66.1, C67.1, C68.1, C69.1, C70.1, PWM_DRIVER2.28, PWM_DRIVER3.28, PWM_DRIVER4.28, PWM_DRIVER5.28, PWM_DRIVER6.28
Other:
- board size 78.3 x 40.6 mm -> 78.3 x 38.4 mm
